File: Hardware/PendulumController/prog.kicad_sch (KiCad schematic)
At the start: 16 parts, among them J401 USBC, J402 PROG, U401 FT232RL

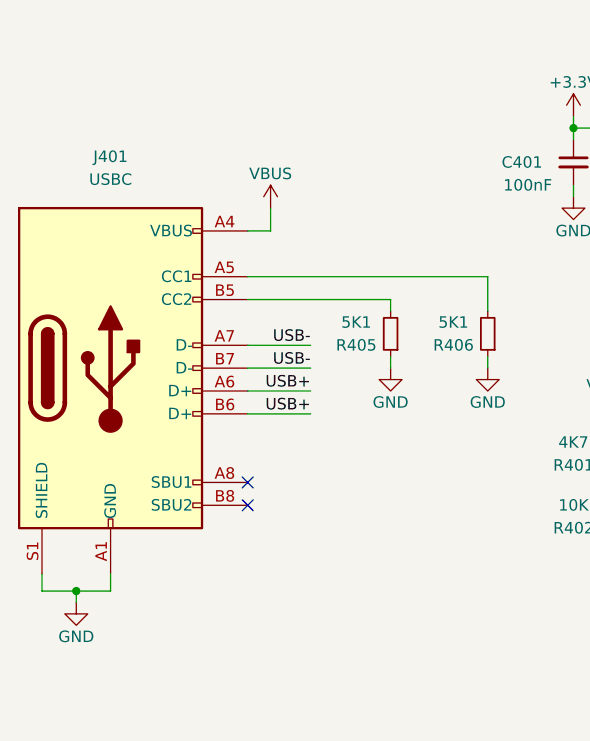
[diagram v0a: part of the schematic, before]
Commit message: Add power flags
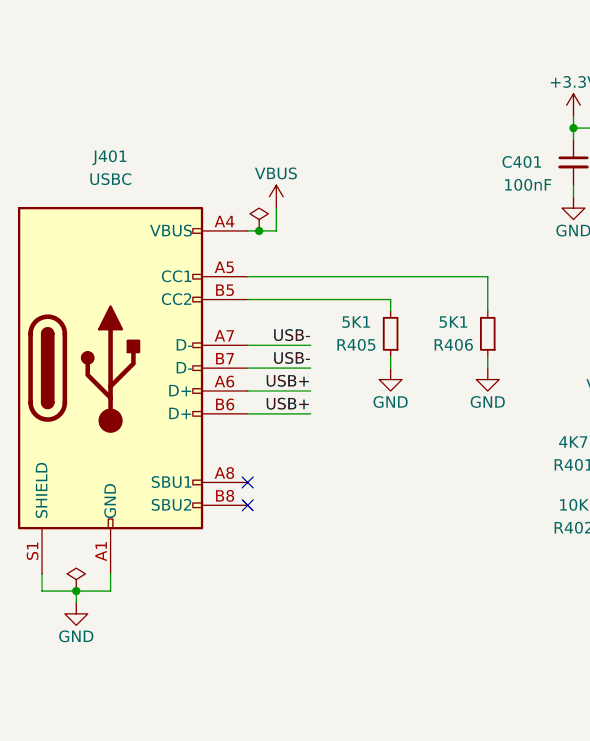
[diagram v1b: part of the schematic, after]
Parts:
- J401: footprint (none) -> Connector_USB:USB_C_Receptacle_XKB_U262-16XN-4BVC11
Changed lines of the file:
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@@
   (junction (at 50.8 120.65) (diameter 0) (color 0 0 0 0)
+  )
+  (junction (at 71.12 80.645) (diameter 0) (color 0 0 0 0)
   )
   (junction (at 135.89 67.945) (diameter 0) (color 0 0 0 0)
@@
     (stroke (width 0) (type default) (color 0 0 0 0))
   )
+  (wire (pts (xy 50.8 120.65) (xy 54.61 120.65))
+    (stroke (width 0) (type default) (color 0 0 0 0))
+  )
   (wire (pts (xy 106.045 69.215) (xy 125.095 69.215))
     (stroke (width 0) (type default) (color 0 0 0 0))
@@
     (stroke (width 0) (type default) (color 0 0 0 0))
   )
-  (wire (pts (xy 72.39 80.645) (xy 72.39 78.105))
+  (wire (pts (xy 73.025 80.645) (xy 73.025 78.105))
     (stroke (width 0) (type default) (color 0 0 0 0))
   )
@@
     (stroke (width 0) (type default) (color 0 0 0 0))
   )
+  (wire (pts (xy 71.12 80.645) (xy 73.025 80.645))
+    (stroke (width 0) (type default) (color 0 0 0 0))
+  )
   (wire (pts (xy 125.095 84.455) (xy 130.81 84.455))
     (stroke (width 0) (type default) (color 0 0 0 0))
@@
     (stroke (width 0) (type default) (color 0 0 0 0))
   )
-  (wire (pts (xy 69.85 80.645) (xy 72.39 80.645))
+  (wire (pts (xy 69.85 80.645) (xy 71.12 80.645))
     (stroke (width 0) (type default) (color 0 0 0 0))
   )
@@
   )
   (wire (pts (xy 120.65 94.615) (xy 130.81 94.615))
-    (stroke (width 0) (type default) (color 0 0 0 0))
-  )
-  (wire (pts (xy 50.8 120.65) (xy 54.61 120.65))
     (stroke (width 0) (type default) (color 0 0 0 0))
   )
@@
     (property "Reference" "J401" (id 0) (at 54.61 72.39 0))
     (property "Value" "USBC" (id 1) (at 54.61 74.93 0))
-    (property "Footprint" "" (id 2) (at 58.42 95.885 0)
+    (property "Footprint" "Connector_USB:USB_C_Receptacle_XKB_U262-16XN-4BVC11" (id 2) (at 58.42 95.885 0)
       (effects (font (size 1.27 1.27)) hide)
     )
@@
     (pin "2")
   )
+  (symbol (lib_id "power:PWR_FLAG") (at 50.8 120.65 0) (unit 1)
+    (in_bom yes) (on_board yes) (fields_autoplaced)
+    (property "Reference" "#FLG0103" (id 0) (at 50.8 118.745 0)
+      (effects (font (size 1.27 1.27)) hide)
+    )
+    (property "Value" "PWR_FLAG" (id 1) (at 50.8 114.935 0)
+      (effects (font (size 1.27 1.27)) hide)
+    )
+    (property "Footprint" "" (id 2) (at 50.8 120.65 0)
+      (effects (font (size 1.27 1.27)) hide)
+    )
+    (property "Datasheet" "~" (id 3) (at 50.8 120.65 0)
+      (effects (font (size 1.27 1.27)) hide)
+    )
+    (pin "1")
+  )
   (symbol (lib_id "power:VBUS") (at 109.855 101.6 0) (unit 1)
     (in_bom yes) (on_board yes)
@@
     (pin "2")
   )
-  (symbol (lib_id "power:VBUS") (at 72.39 78.105 0) (unit 1)
-    (in_bom yes) (on_board yes)
-    (property "Reference" "#PWR0129" (id 0) (at 72.39 81.915 0)
-      (effects (font (size 1.27 1.27)) hide)
-    )
-    (property "Value" "VBUS" (id 1) (at 72.39 74.295 0))
-    (property "Footprint" "" (id 2) (at 72.39 78.105 0)
-      (effects (font (size 1.27 1.27)) hide)
-    )
-    (property "Datasheet" "" (id 3) (at 72.39 78.105 0)
-      (effects (font (size 1.27 1.27)) hide)
-    )
+  (symbol (lib_id "power:VBUS") (at 73.025 78.105 0) (unit 1)
+    (in_bom yes) (on_board yes)
+    (property "Reference" "#PWR0129" (id 0) (at 73.025 81.915 0)
+      (effects (font (size 1.27 1.27)) hide)
+    )
+    (property "Value" "VBUS" (id 1) (at 73.025 74.295 0))
+    (property "Footprint" "" (id 2) (at 73.025 78.105 0)
+      (effects (font (size 1.27 1.27)) hide)
+    )
+    (property "Datasheet" "" (id 3) (at 73.025 78.105 0)
+      (effects (font (size 1.27 1.27)) hide)
+    )
+    (pin "1")
+  )
+  (symbol (lib_id "power:PWR_FLAG") (at 71.12 80.645 0) (unit 1)
+    (in_bom yes) (on_board yes) (fields_autoplaced)
+    (property "Reference" "#FLG0102" (id 0) (at 71.12 78.74 0)
+      (effects (font (size 1.27 1.27)) hide)
+    )
+    (property "Value" "PWR_FLAG" (id 1) (at 71.12 74.93 0)
+      (effects (font (size 1.27 1.27)) hide)
+    )
+    (property "Footprint" "" (id 2) (at 71.12 80.645 0)
+      (effects (font (size 1.27 1.27)) hide)
+    )
+    (property "Datasheet" "~" (id 3) (at 71.12 80.645 0)
+      (effects (font (size 1.27 1.27)) hide)
+    )

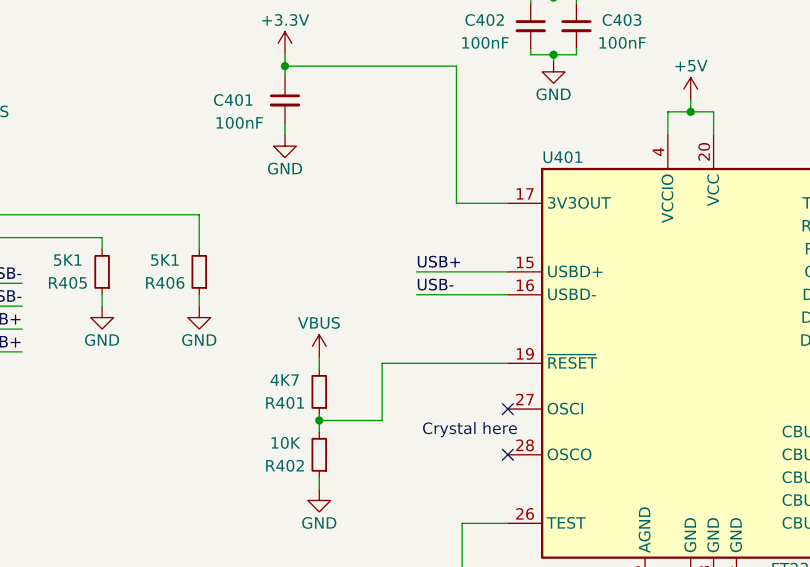
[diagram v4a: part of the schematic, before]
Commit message: Add usb terminators
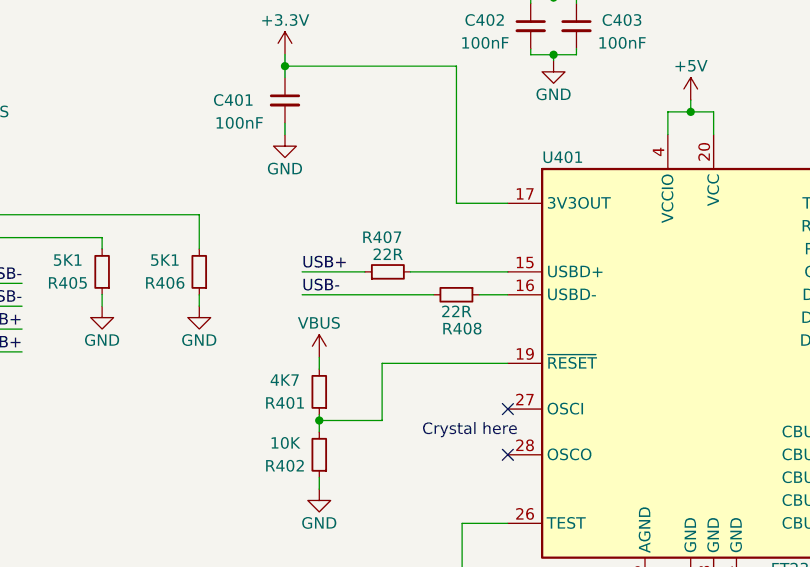
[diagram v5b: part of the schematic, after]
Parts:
- added R407, R408: 22R, Resistor_SMD:R_0805_2012Metric, symbol Device:R_Small
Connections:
- net USB+: now also R407.1; no longer U401.15 (USBD+)
- net USB-: now also R408.2; no longer U401.16 (USBD-)
- new net: R407.2, U401.15 (USBD+)
- new net: R408.1, U401.16 (USBD-)
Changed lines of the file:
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@@
     (stroke (width 0) (type default) (color 0 0 0 0))
   )
-  (wire (pts (xy 120.65 92.075) (xy 130.81 92.075))
+  (wire (pts (xy 107.95 92.075) (xy 114.935 92.075))
     (stroke (width 0) (type default) (color 0 0 0 0))
   )
@@
     (stroke (width 0) (type default) (color 0 0 0 0))
   )
-  (wire (pts (xy 120.65 94.615) (xy 130.81 94.615))
+  (wire (pts (xy 107.95 94.615) (xy 122.555 94.615))
     (stroke (width 0) (type default) (color 0 0 0 0))
   )
@@
     (stroke (width 0) (type default) (color 0 0 0 0))
   )
+  (wire (pts (xy 120.015 92.075) (xy 130.81 92.075))
+    (stroke (width 0) (type default) (color 0 0 0 0))
+  )
   (wire (pts (xy 182.88 112.395) (xy 196.85 112.395))
     (stroke (width 0) (type default) (color 0 0 0 0))
@@
   )
   (wire (pts (xy 109.855 101.6) (xy 109.855 102.87))
+    (stroke (width 0) (type default) (color 0 0 0 0))
+  )
+  (wire (pts (xy 127.635 94.615) (xy 130.81 94.615))
     (stroke (width 0) (type default) (color 0 0 0 0))
   )
@@
     (effects (font (size 1.27 1.27)) (justify right bottom))
   )
-  (label "USB+" (at 120.65 92.075 0)
+  (label "USB+" (at 107.95 92.075 0)
     (effects (font (size 1.27 1.27)) (justify left bottom))
   )
@@
     (effects (font (size 1.27 1.27)) (justify right bottom))
   )
-  (label "USB-" (at 120.65 94.615 0)
+  (label "USB-" (at 107.95 94.615 0)
     (effects (font (size 1.27 1.27)) (justify left bottom))
   )
@@
     (pin "1")
   )
+  (symbol (lib_id "Device:R_Small") (at 117.475 92.075 90) (unit 1)
+    (in_bom yes) (on_board yes)
+    (property "Reference" "R407" (id 0) (at 116.84 88.265 90))
+    (property "Value" "22R" (id 1) (at 117.475 90.17 90))
+    (property "Footprint" "Resistor_SMD:R_0805_2012Metric" (id 2) (at 117.475 92.075 0)
+      (effects (font (size 1.27 1.27)) hide)
+    )
+    (property "Datasheet" "~" (id 3) (at 117.475 92.075 0)
+      (effects (font (size 1.27 1.27)) hide)
+    )
+    (pin "1")
+    (pin "2")
+  )
   (symbol (lib_id "Device:LED") (at 193.04 109.855 0) (unit 1)
     (in_bom yes) (on_board yes)
@@
     (pin "1")
   )
+  (symbol (lib_id "Device:R_Small") (at 125.095 94.615 270) (unit 1)
+    (in_bom yes) (on_board yes)
+    (property "Reference" "R408" (id 0) (at 125.73 98.425 90))
+    (property "Value" "22R" (id 1) (at 125.095 96.52 90))
+    (property "Footprint" "Resistor_SMD:R_0805_2012Metric" (id 2) (at 125.095 94.615 0)
+      (effects (font (size 1.27 1.27)) hide)
+    )
+    (property "Datasheet" "~" (id 3) (at 125.095 94.615 0)
+      (effects (font (size 1.27 1.27)) hide)
+    )
+    (pin "1")
+    (pin "2")
+  )
   (symbol (lib_name "GND_5") (lib_id "power:GND") (at 85.725 95.885 0) (unit 1)

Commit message: Firmware (#15)
Merged for PRR
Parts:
- added D403: MBR0520, Diode_SMD:D_SOD-123, symbol Diode:MBR0520
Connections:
- net +5V: now also D403.1 (K)
- net VBUS: now also D403.2 (A)
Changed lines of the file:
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@@
+    (stroke (width 0) (type default) (color 0 0 0 0))
+  )
+  (wire (pts (xy 79.375 52.705) (xy 85.09 52.705))
     (stroke (width 0) (type default) (color 0 0 0 0))
   )
@@
     (stroke (width 0) (type default) (color 0 0 0 0))
   )
+  (wire (pts (xy 99.06 52.705) (xy 99.06 50.8))
+    (stroke (width 0) (type default) (color 0 0 0 0))
+  )
   (wire (pts (xy 50.8 120.65) (xy 54.61 120.65))
     (stroke (width 0) (type default) (color 0 0 0 0))
@@
     (stroke (width 0) (type default) (color 0 0 0 0))
   )
+  (wire (pts (xy 79.375 50.8) (xy 79.375 52.705))
+    (stroke (width 0) (type default) (color 0 0 0 0))
+  )
   (wire (pts (xy 135.89 67.945) (xy 138.43 67.945))
     (stroke (width 0) (type default) (color 0 0 0 0))
@@
   )
   (wire (pts (xy 133.35 62.23) (xy 133.35 61.595))
+    (stroke (width 0) (type default) (color 0 0 0 0))
+  )
+  (wire (pts (xy 92.71 52.705) (xy 99.06 52.705))
     (stroke (width 0) (type default) (color 0 0 0 0))
   )
@@
     )
     (property "Datasheet" "~" (id 3) (at 96.52 92.075 0)
+      (effects (font (size 1.27 1.27)) hide)
+    )
+    (pin "1")
+    (pin "2")
+  )
+  (symbol (lib_id "Diode:MBR0520") (at 88.9 52.705 180) (unit 1)
+    (in_bom yes) (on_board yes)
+    (property "Reference" "D403" (id 0) (at 88.9 47.625 0))
+    (property "Value" "MBR0520" (id 1) (at 88.9 50.165 0))
+    (property "Footprint" "Diode_SMD:D_SOD-123" (id 2) (at 88.9 48.26 0)
+      (effects (font (size 1.27 1.27)) hide)
+    )
+    (property "Datasheet" "http://www.mccsemi.com/up_pdf/MBR0520~MBR0580(SOD123).pdf" (id 3) (at 88.9 52.705 0)
       (effects (font (size 1.27 1.27)) hide)
     )
@@
     (pin "5")
     (pin "6")
+  )
+  (symbol (lib_name "VBUS_1") (lib_id "power:VBUS") (at 79.375 50.8 0) (unit 1)
+    (in_bom yes) (on_board yes)
+    (property "Reference" "#PWR0148" (id 0) (at 79.375 54.61 0)
+      (effects (font (size 1.27 1.27)) hide)
+    )
+    (property "Value" "VBUS" (id 1) (at 79.375 46.99 0))
+    (property "Footprint" "" (id 2) (at 79.375 50.8 0)
+      (effects (font (size 1.27 1.27)) hide)
+    )
+    (property "Datasheet" "" (id 3) (at 79.375 50.8 0)
+      (effects (font (size 1.27 1.27)) hide)
+    )
+    (pin "1")
   )
   (symbol (lib_id "Device:C_Small") (at 106.045 73.025 0) (unit 1)
@@
     (pin "2")
   )
+  (symbol (lib_name "+5V_3") (lib_id "power:+5V") (at 99.06 50.8 0) (unit 1)
+    (in_bom yes) (on_board yes) (fields_autoplaced)
+    (property "Reference" "#PWR0147" (id 0) (at 99.06 54.61 0)
+      (effects (font (size 1.27 1.27)) hide)
+    )
+    (property "Value" "+5V" (id 1) (at 99.06 45.72 0))
+    (property "Footprint" "" (id 2) (at 99.06 50.8 0)
+      (effects (font (size 1.27 1.27)) hide)
+    )
+    (property "Datasheet" "" (id 3) (at 99.06 50.8 0)
+      (effects (font (size 1.27 1.27)) hide)
+    )
+    (pin "1")
+  )
   (symbol (lib_name "+5V_3") (lib_id "power:+5V") (at 138.43 45.72 0) (unit 1)
